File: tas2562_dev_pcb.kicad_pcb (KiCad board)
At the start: 4 copper layers, 29.2 x 36.8 mm, 26 parts, among them J1 Conn_01x10_Female, J3 Screw_Terminal_01x02, J4 Conn_01x10_Female, U1 LM1117-1.8, U2 TAS2562

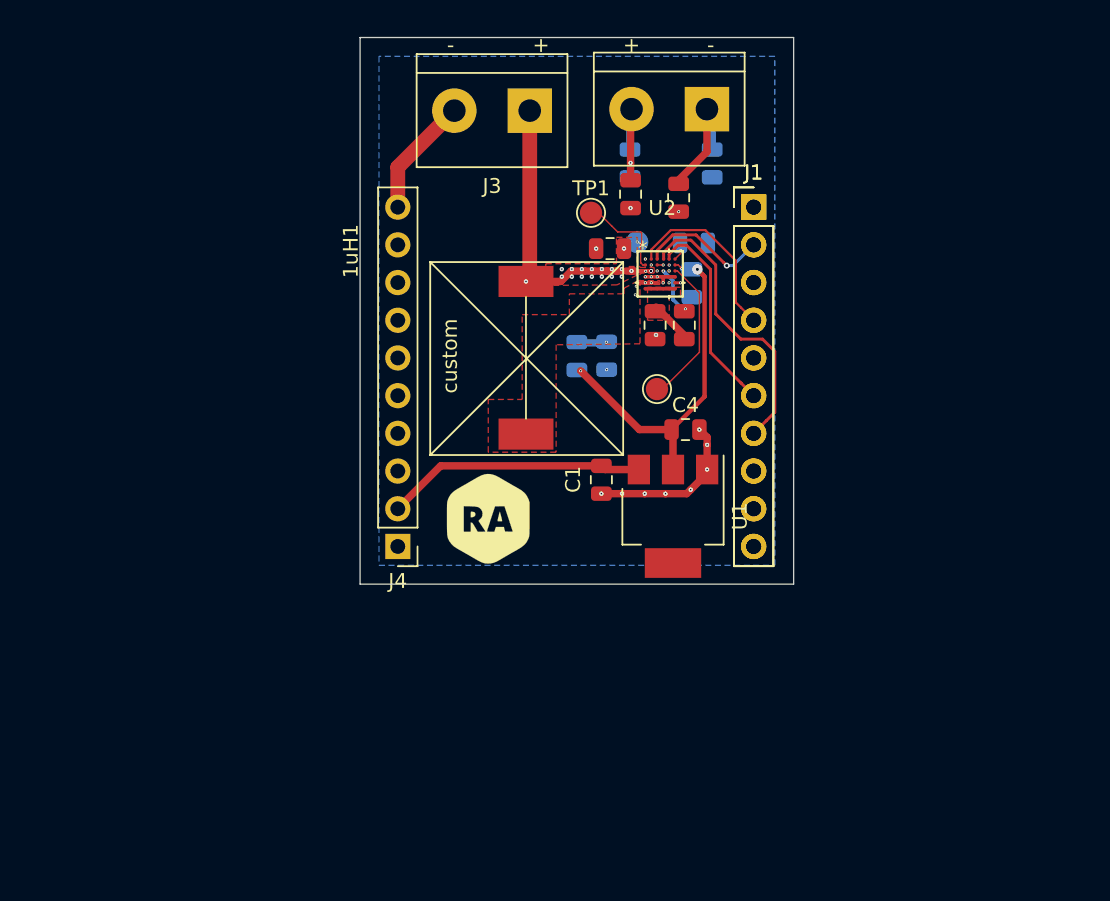
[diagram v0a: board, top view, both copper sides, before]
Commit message: added gerber, layout done in 2layers
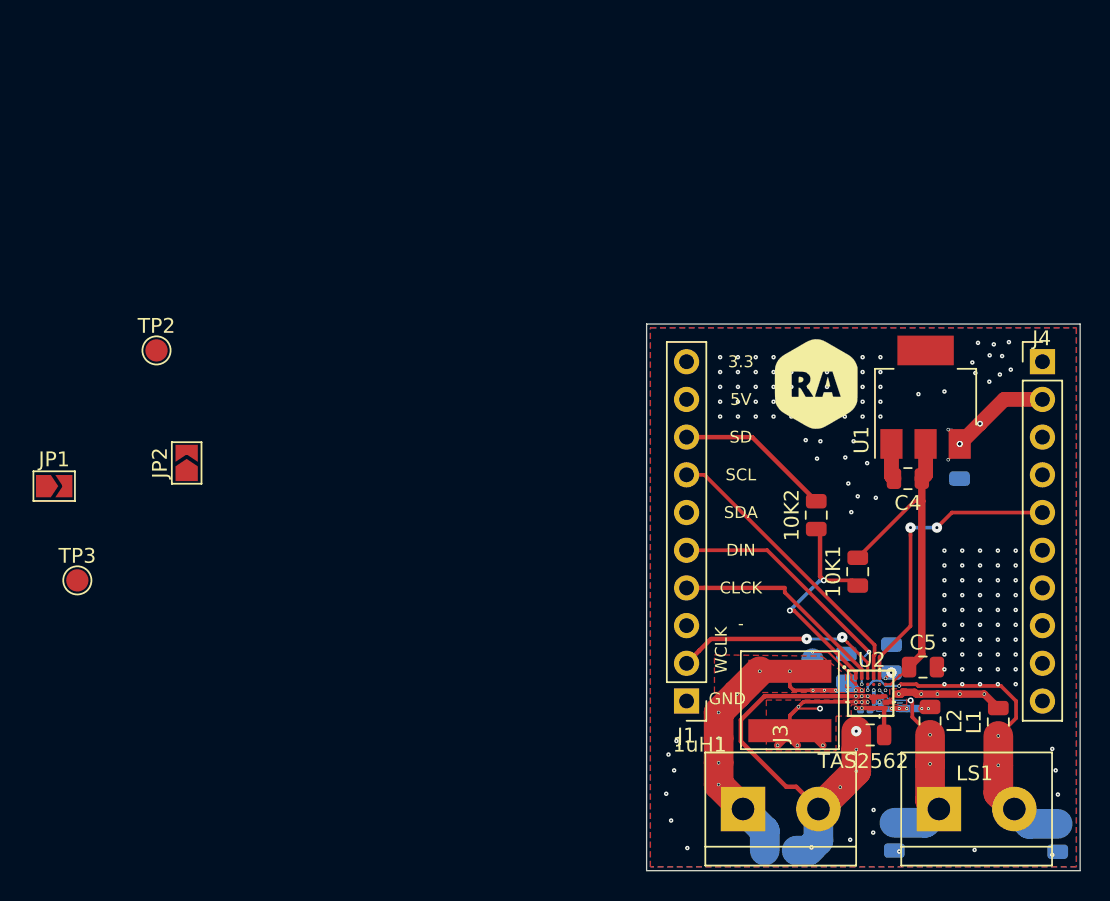
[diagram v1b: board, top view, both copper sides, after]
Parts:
- removed 100nF1: 100nF, Capacitor_SMD:C_0805_2012Metric
- removed the G*** at (135.6, 91.9)
- removed the G*** at (147.6, 91.4)
- removed the J1 at (153.5, 69.8)
- added 100nF: 100nF, Capacitor_SMD:C_0201_0603Metric, B.Cu at (161.0, 103.8)
- added C9: 10uF, Capacitor_SMD:C_0805_2012Metric, B.Cu at (155.2, 113.2)
- added G***: LOGO, logos:rodaawana, F.Cu at (157.7, 82.9)
- added JP1: Jumper, Jumper:SolderJumper-2_P1.3mm_Open_TrianglePad1.0x1.5mm, F.Cu at (106.4, 88.6)
- added JP2: Jumper, Jumper:SolderJumper-2_P1.3mm_Open_TrianglePad1.0x1.5mm, F.Cu at (115.3, 87.1)
- 10K1, 10K2, C5, TP2: moved to F.Cu
- 1uH1: footprint Inductor_SMD:1212_wurth -> Inductor_SMD:6.6-6.4
- C1, C8, TP1: moved to B.Cu
- moved C3 53.8 mm to (174.0, 112.3)
- moved LS1 49.7 mm to (166.0, 110.4), turned to 0 degrees
- moved J3 49.2 mm to (152.8, 110.4), turned to 0 degrees
- moved C2 47.0 mm to (163.0, 112.3)
- moved J4 45.2 mm to (173.0, 80.3), turned to 0 degrees
- moved L1 43.3 mm to (170.0, 104.5), turned to 90 degrees
- moved TP3 41.1 mm to (108.0, 95.0)
- moved L2 39.1 mm to (165.4, 104.5), turned to 270 degrees
- moved TP1 33.6 mm to (157.5, 100.3)
- moved J1 33.6 mm to (149.0, 103.1), turned to 180 degrees
- moved TP2 33.2 mm to (113.3, 79.5)
- moved C8 32.4 mm to (159.8, 100.9), turned to 270 degrees
- moved U2 31.6 mm to (161.4, 102.6)
- moved C6 31.2 mm to (161.4, 105.4), turned to 180 degrees
- moved C7 31.0 mm to (162.8, 100.3), turned to 270 degrees
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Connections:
- L1 pad 2: SPK_P -> SPK_N
- L2 pad 1: SPK_N -> SPK_P
- U2 pad B3: GNDREF -> Net-(JP2-Pad2)
- U2 pad B4: GNDREF -> Net-(JP1-Pad2)
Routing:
- net 5v_Ext: track 41.5 -> 9.74 mm, vias 0 -> 5
- net Net-(J1-Pad10): track 24.0 -> 0.00 mm
- net ~SHUTDOWN: track 29.6 -> 10.5 mm, vias 1 -> 0
- net GNDREF: track 24.2 -> 35.7 mm, vias 15 -> 141
- net Net-(1uH1-Pad2): track 5.12 -> 15.7 mm, vias 4 -> 8
- net Net-(TP3-Pad1): track 10.1 -> 0.00 mm, vias 0 -> 1
- net Net-(C2-Pad1): track 20.5 -> 13.9 mm, vias 1 -> 4
- net SDA: track 13.7 -> 20.3 mm, vias 0 -> 2
- net Net-(C3-Pad1): track 16.2 -> 22.6 mm, vias 2 -> 8
- net SPK_P: track 11.4 -> 5.46 mm, vias 2 -> 6
- net WCLK: track 8.94 -> 14.7 mm, vias 1 -> 2
- net VIN: track 24.9 -> 28.7 mm, vias 24 -> 13
- net SPK_N: track 5.74 -> 8.78 mm, vias 2 -> 5
- net Net-(TP2-Pad1): track 3.07 -> 0.06 mm, vias 2 -> 1
- net CLCK: track 12.2 -> 14.9 mm
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- added copper zone on F.Cu, net GNDREF
- added copper zone on F.Cu, net SPK_N
- added copper zone on B.Cu, net SPK_P
- removed copper zone on F.Cu, net Net-(100nF1-Pad1)
- removed copper zone on In1.Cu, net VIN
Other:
- copper layers 4 -> 2
- net class Default: clearance 0.15 -> 0.1; trace_width 0.2 -> 0.15
- rule trace_clearance: 0.15 -> 0.1
- board text added: "3.3"
- board text added: "5V"
- board text added: "CLCK"
- board text added: "SD"
- board text added: "TAS2562 v1.0 By:Manojkumar"
- board text removed: "+"
- board text removed: "3.3vEXT"
- board text removed: "5VEXT"
- board text removed: "BCLK"
- board text removed: "SDWN"
